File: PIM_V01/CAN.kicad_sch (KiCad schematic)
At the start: 40 parts, among them U4 MCP2562FDT-E/SN, U5 MCP2562FDT-E/SN

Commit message: updated some of the 3D bodies, and updated the BRINGUP plan with results from the first attempt at population; many components were not made in the order, so am now blocked waiting for those.
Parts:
- C10, C11, C14, C15: MPN (none) -> MSAST168BB5475MTNA01; PD (none) -> CAP CER 4.7UF 25V X5R 0603
- C12, C13, C16, C17: MPN (none) -> GCM188R71H104KA57D; PD (none) -> CAP CER 0.1UF 50V X7R 0603
- C18, C19, C20, C21: MPN (none) -> GCM1885C1H470JA16D; PD (none) -> CAP CER 47PF 50V C0G/NP0 0603
- C22, C23, C24, C25: MPN (none) -> GCM1885C1H470JA16D; PD (none) -> CAP CER 47PF 50V C0G/NP0 0603; now fitted
- C26, C27: MPN (none) -> GCM1885C1H472GA16D; PD (none) -> CAP CER 4700PF 50V C0G/NP0 0603
- D7, D8: MPN (none) -> ESD16VHYFHT116; PD (none) -> TVS DIODE 12VWM SOT23; now fitted
- FL1, FL2: MPN (none) -> ACT45B-101-2P-TL003; PD (none) -> CMC 100UH 150MA 2LN 5.8KOHM SMD
- R14, R15: MPN (none) -> ERJ-3EKF1002V; PD (none) -> RES SMD 10K OHM 1% 1/10W 0603
- R16, R17: MPN (none) -> ERJ-3GEY0R00V; PD (none) -> RES SMD 0 OHM JUMPER 1/10W 0603
- R18, R19, R20, R21: MPN (none) -> ERJ-3EKF60R4V; PD (none) -> RES SMD 60.4 OHM 1% 1/10W 0603
- R41, R42, R43, R44: MPN (none) -> ERJ-3EKF1001V; PD (none) -> RES SMD 1K OHM 1% 1/10W 0603
- U4, U5: MPN (none) -> MCP2562FDT-E/SN; PD (none) -> IC TRANSCEIVER 1/1 8SOIC
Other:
- note added: "60.4 FOR DEV ..."

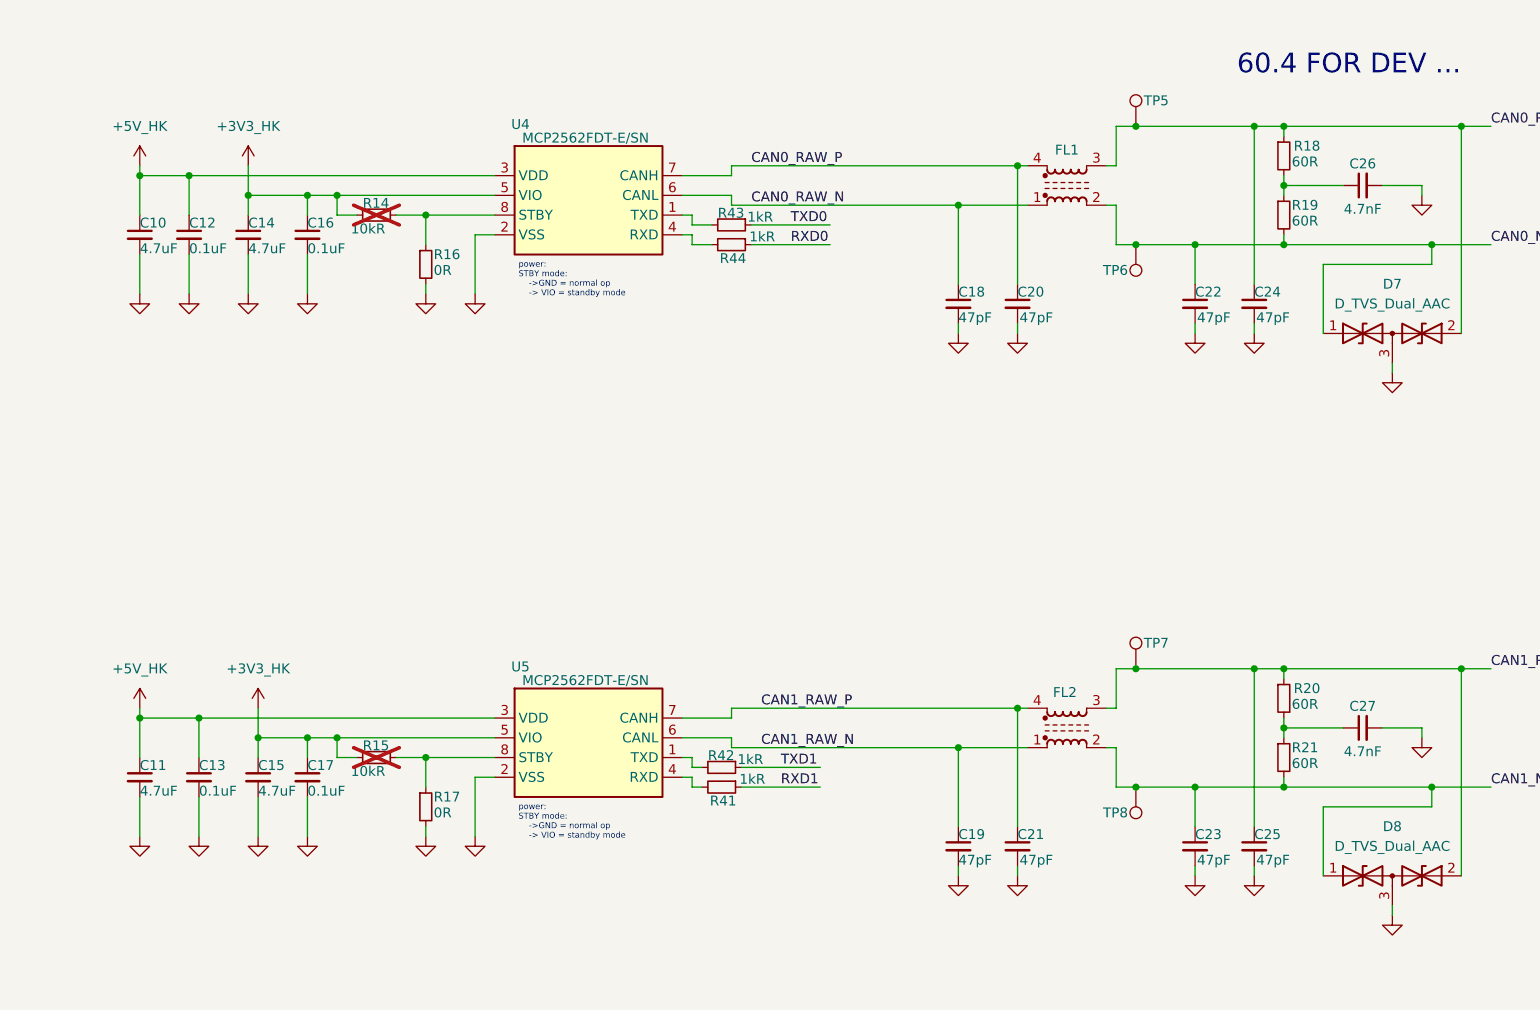
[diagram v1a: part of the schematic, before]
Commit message: finished uploading all of the correct footprints and 3D bodies. this is now done, and barely different than what was fabricated - used all manufacturers FPs (instead of kicads), but this didn't cause any of the original connections to break. I will now start on V02 (incl FPGA and smaller)
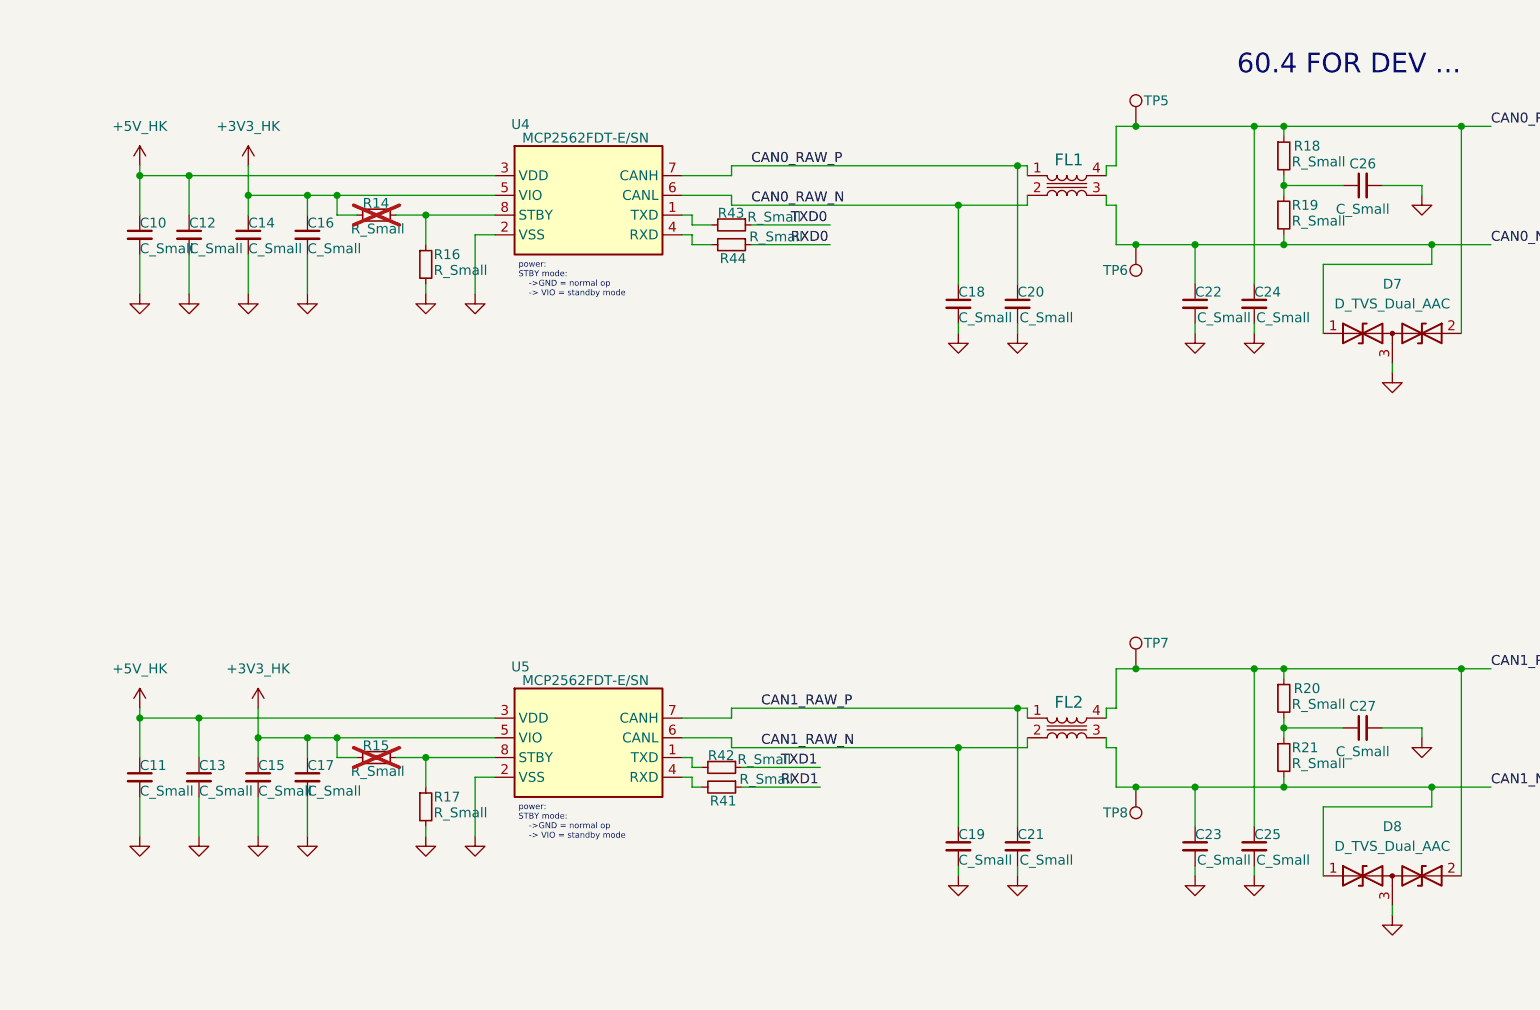
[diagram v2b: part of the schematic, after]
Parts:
- removed FL1, FL2: Choke_CommonMode_FerriteCore_1243, Inductor_SMD:L_CommonModeChoke_Coilcraft_1812CAN, symbol Filter:Choke_CommonMode_FerriteCore_1243
- added FL1, FL2: ACT45B-101-2P-TL003, CustomFootprints:ACT45B-101-2P-TL003_TDK, symbol Custom_Components:ACT45B-101-2P-TL003
- C10, C11, C14, C15: value 4.7uF -> C_Small
- C12, C13, C16, C17: value 0.1uF -> C_Small
- C18, C19, C20, C21, C22, C23, C24, C25: value 47pF -> C_Small
- C26, C27: value 4.7nF -> C_Small
- R14, R15: value 10kR -> R_Small
- R16, R17: value 0R -> R_Small
- R18, R19, R20, R21: value 60R -> R_Small
- R41, R42, R43, R44: value 1kR -> R_Small
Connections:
- net CAN0_N: now also FL1.3
- net CAN0_P: now also FL1.4
- net CAN0_RAW_N: now also FL1.2
- net CAN0_RAW_P: now also FL1.1
- net CAN1_N: now also FL2.3
- net CAN1_P: now also FL2.4
- net CAN1_RAW_N: now also FL2.2
- net CAN1_RAW_P: now also FL2.1

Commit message: somehow last push my components had lost their values, and only displayed their Kicad value, but I fixed that now
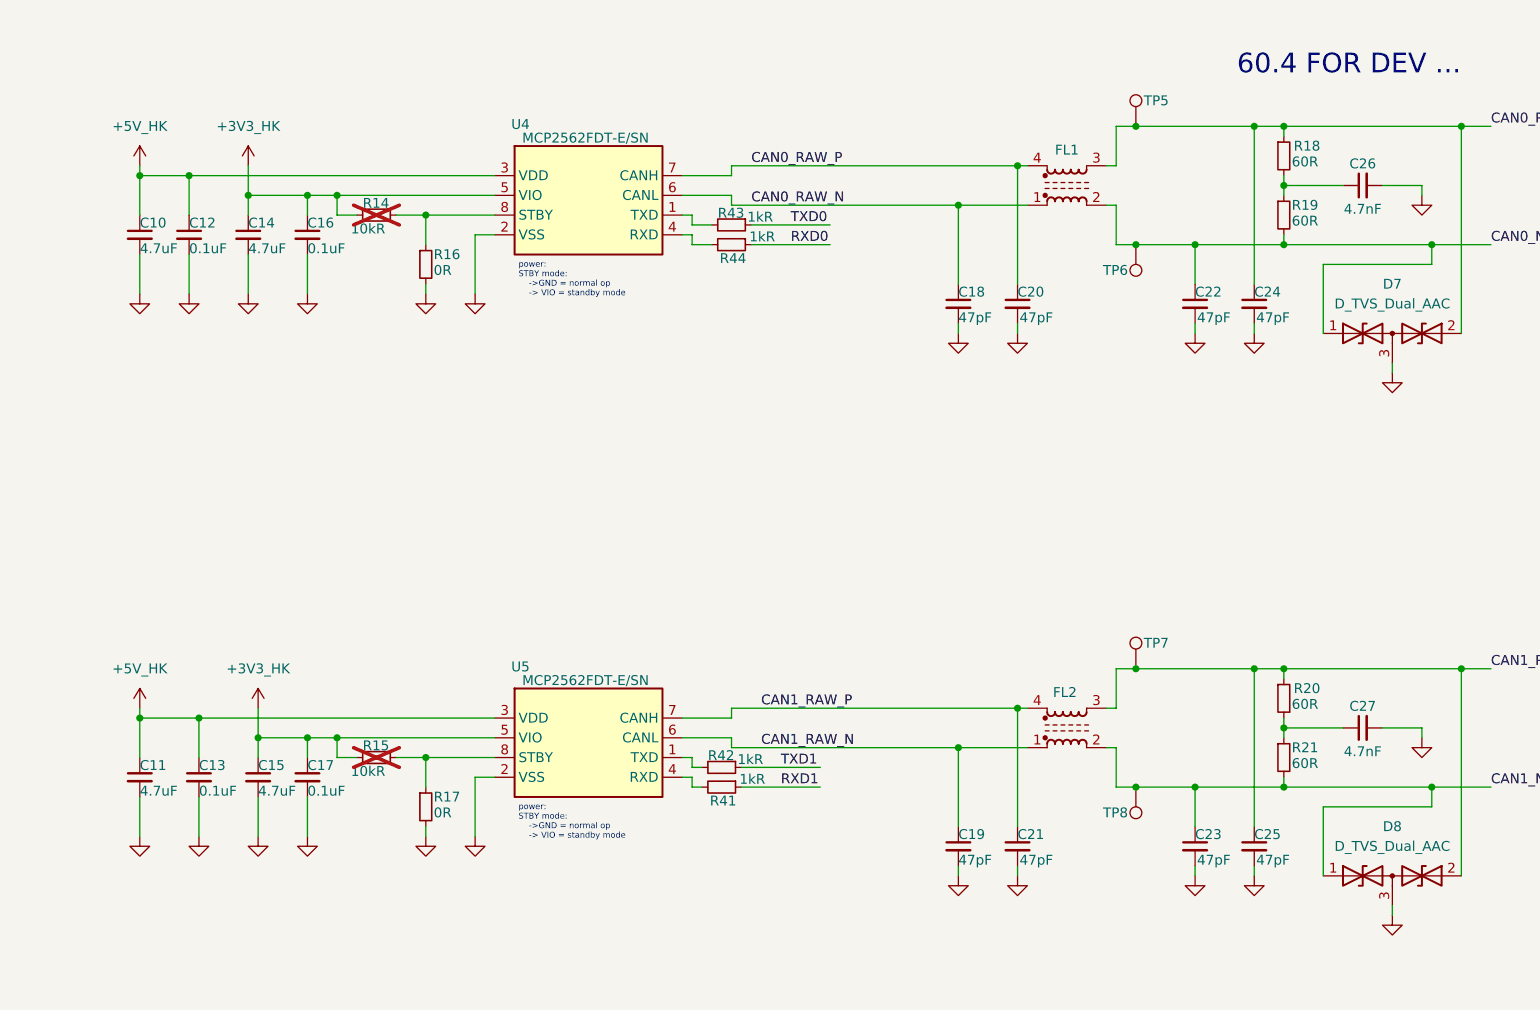
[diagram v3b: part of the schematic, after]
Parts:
- removed FL1, FL2: ACT45B-101-2P-TL003, CustomFootprints:ACT45B-101-2P-TL003_TDK, symbol Custom_Components:ACT45B-101-2P-TL003
- added FL1, FL2: Choke_CommonMode_FerriteCore_1243, Inductor_SMD:L_CommonModeChoke_Coilcraft_1812CAN, symbol Filter:Choke_CommonMode_FerriteCore_1243
- C10, C11, C14, C15: value C_Small -> 4.7uF
- C12, C13, C16, C17: value C_Small -> 0.1uF
- C18, C19, C20, C21, C22, C23, C24, C25: value C_Small -> 47pF
- C26, C27: value C_Small -> 4.7nF
- R14, R15: value R_Small -> 10kR
- R16, R17: value R_Small -> 0R
- R18, R19, R20, R21: value R_Small -> 60R
- R41, R42, R43, R44: value R_Small -> 1kR
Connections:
- net CAN0_N: now also FL1.2
- net CAN0_P: now also FL1.3
- net CAN0_RAW_N: now also FL1.1
- net CAN0_RAW_P: now also FL1.4
- net CAN1_N: now also FL2.2
- net CAN1_P: now also FL2.3
- net CAN1_RAW_N: now also FL2.1
- net CAN1_RAW_P: now also FL2.4
